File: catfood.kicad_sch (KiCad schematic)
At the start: 0 parts

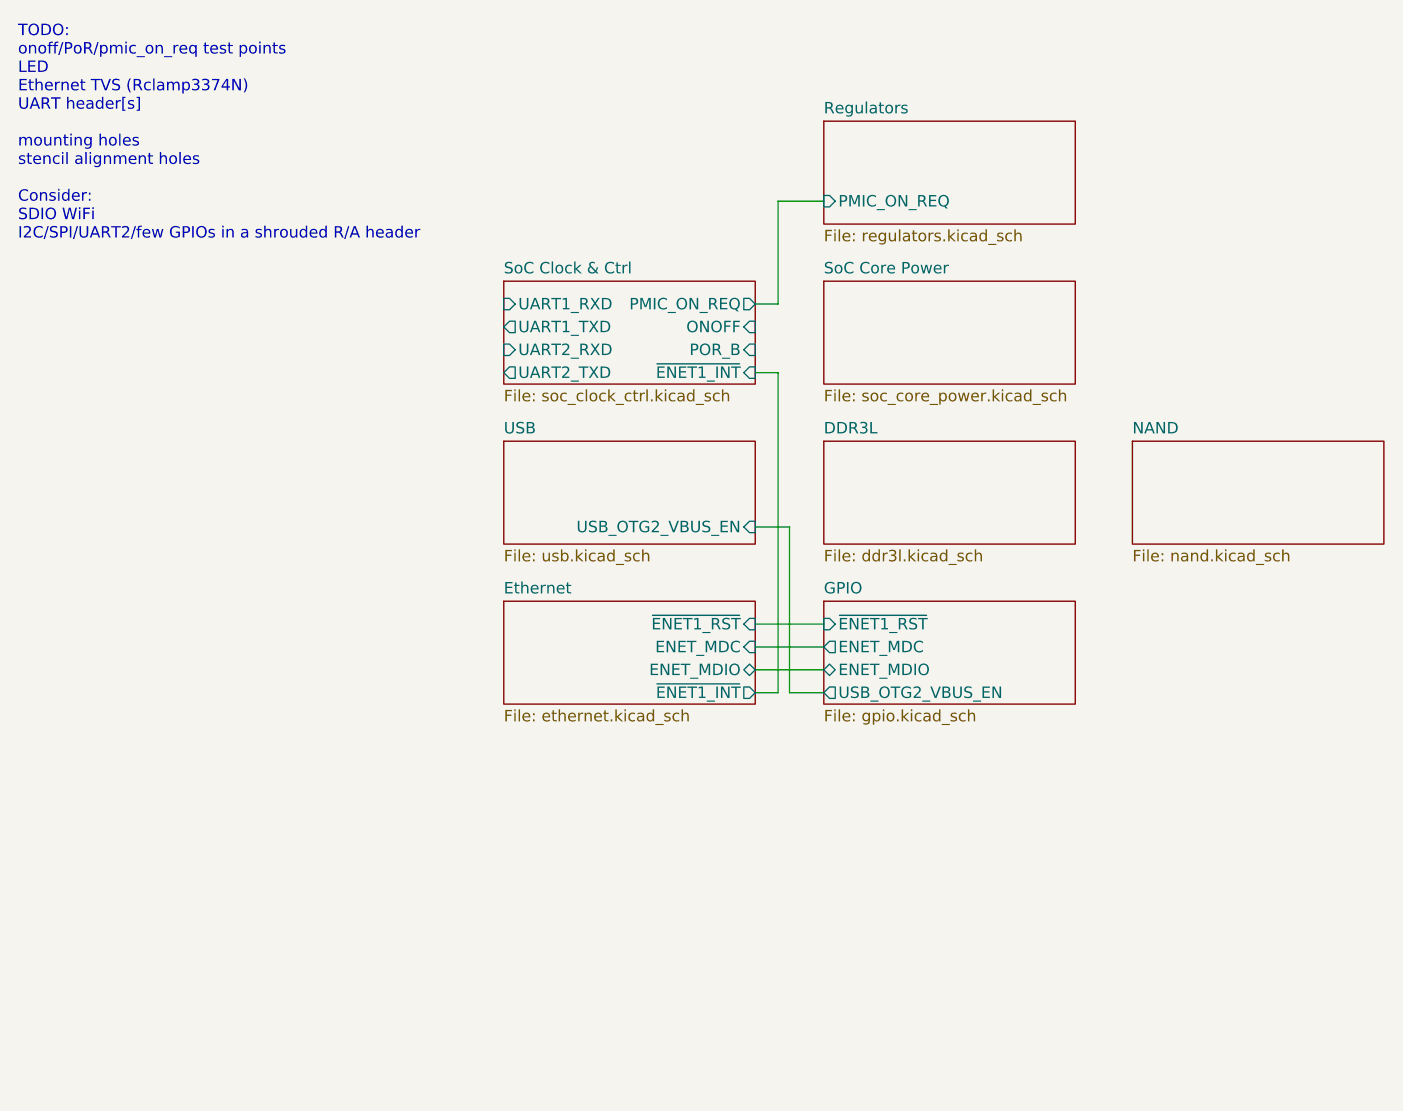
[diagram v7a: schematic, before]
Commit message: Ethernet TVS, UART headers
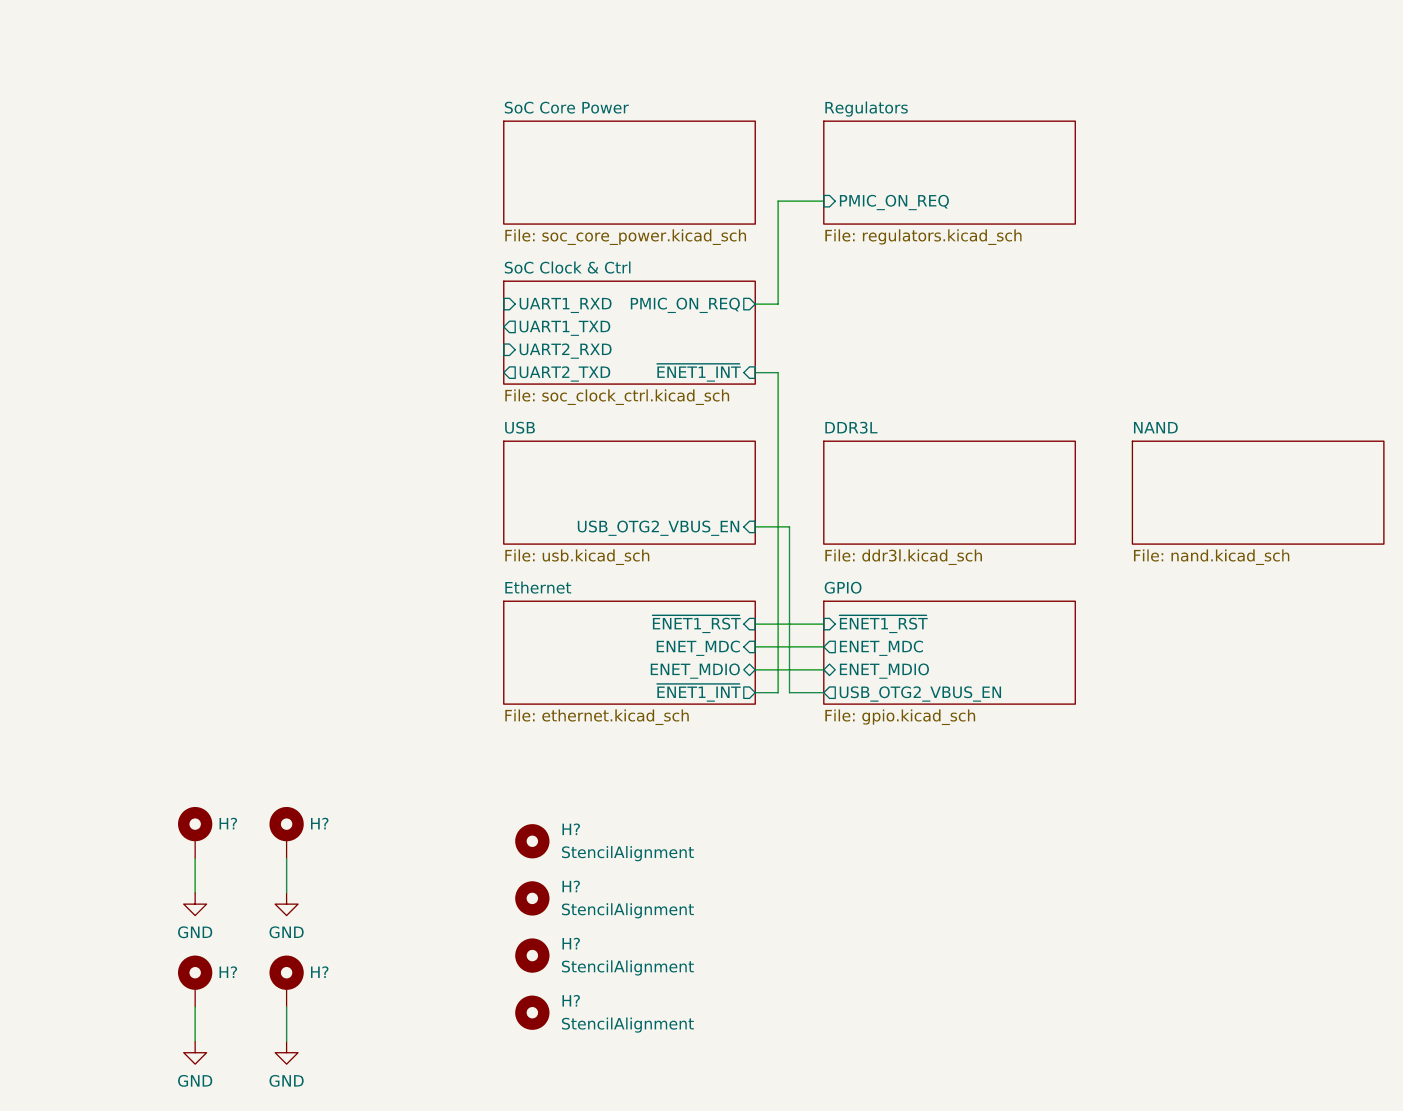
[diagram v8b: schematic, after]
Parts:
- added H? (x4): StencilAlignment, symbol Mechanical:MountingHole
- added H? (x4): MountingHole_Pad, symbol Mechanical:MountingHole_Pad
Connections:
- new net GND: H?.1, H?.1, H?.1, H?.1
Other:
- sheet SoC Clock & Ctrl ports: added none; removed ONOFF, POR_B
- note removed: "TODO: onoff/PoR/pmic_on_req test points LED Ethernet TVS (Rclamp3374N) UART header[s] mounting holes stencil alignment holes Consider: SDIO WiFi I2C/SPI/UART2/few GPIOs in a shrouded R/A header"
